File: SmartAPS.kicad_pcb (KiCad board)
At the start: 2 copper layers, 130 x 60 mm, 102 parts, among them M1 Mechanical-NC, M2 Mechanical-NC, M3 Mechanical-NC, M4 Mechanical, P1 12V IN, P2 GND, P3 OUT1, P4 OUT2, P5 USB_C_Receptacle_16P, P6 JESP32-DBG, Q1 MMBT5551, Q2 DMP3013SFV, Q3 MMBT5551, Q4 DMP3013SFV, Q5 MMBT5551, Q6 DMP3013SFV, Q7 TEMT6000X01, Q8 MMBT5551, U1 MCP1703T-3302E/MB, U2 MUN12AD01-SH, U3 INA226, U4 INA226, U5 IP6510, U6 INA226, U7 SHT20, U8 ESP32-WROOM-32U, U9 STM1001RWX6F

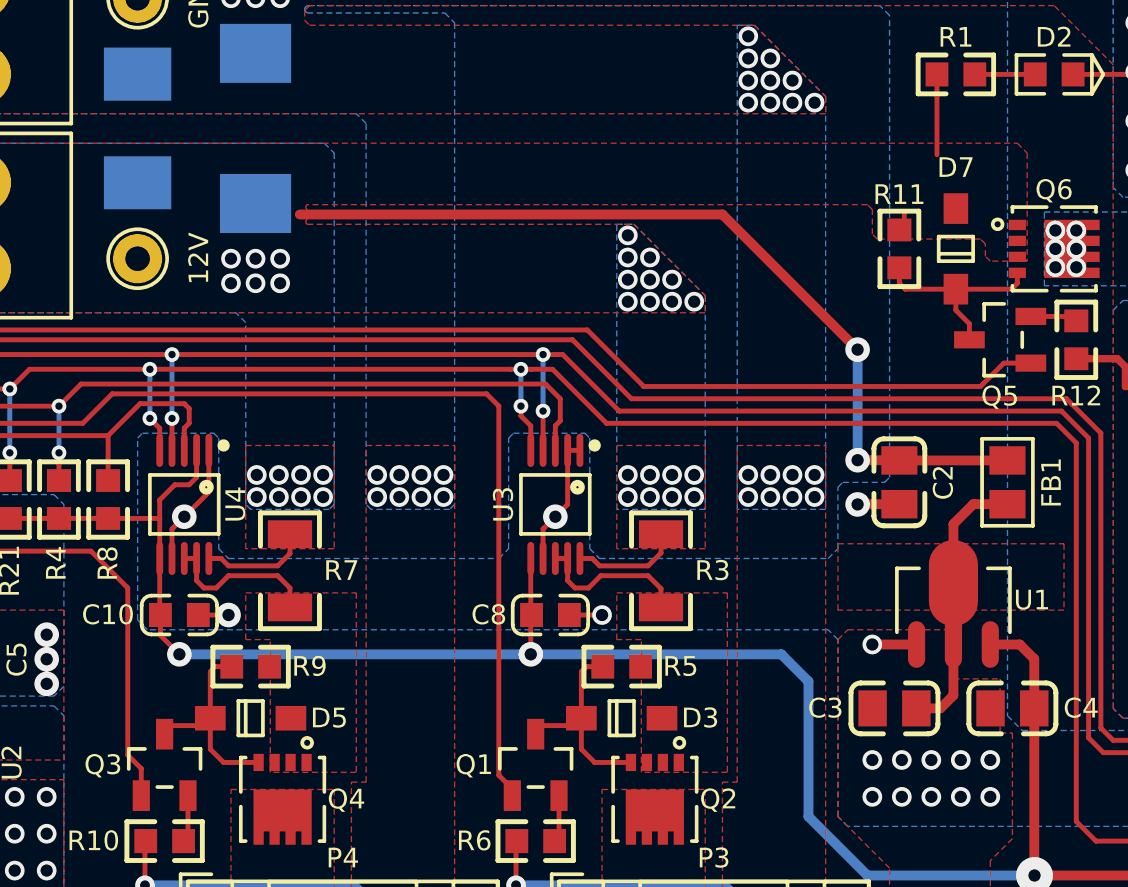
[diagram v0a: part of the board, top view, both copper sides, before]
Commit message: Solve INA226/SHT20 address clash
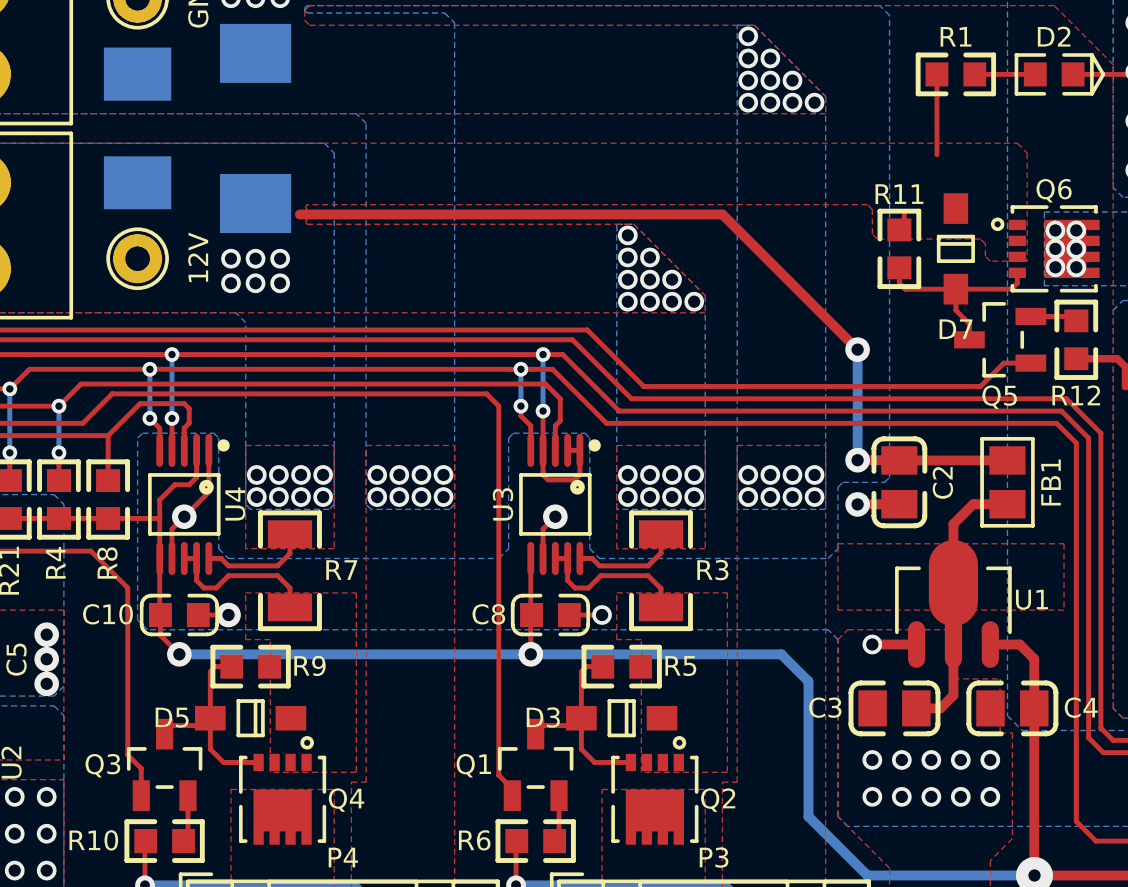
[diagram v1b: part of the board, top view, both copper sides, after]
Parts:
- turned D3 to 180 degrees
- turned D5 to 180 degrees
- turned D7 to 270 degrees
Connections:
- U3 pad 1: GND -> /SDA
- U3 pad 2: GND -> /SDA
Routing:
- net /SDA: track 156.1 -> 160.2 mm
- net GND: track 202.6 -> 199.2 mm

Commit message: Bug fixes, Remove SHT20
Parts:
- removed the C22 at (111.0, 86.0)
- removed the C25 at (226.1, 113.0)
- removed the TP4 at (210.7, 105.1)
- removed the TP5 at (208.7, 105.1)
- removed TP8: SCL, BZ_Misc:TE_RCT0805
- removed TP9: SDA, BZ_Misc:TE_RCT0805
- removed the U7 at (223.0, 113.0)
- added P7: Grove I2C, BZ_Connector:JST_S4B-PH-SM4-TB, F.Cu at (225.0, 116.5)
- added R23: 10K, BZ_Resistor:R_0603, F.Cu at (140.3, 124.2)
- added R24: 10K, BZ_Resistor:R_0603, F.Cu at (142.8, 124.2)
- moved C20 15.0 mm to (202.7, 120.0)
- moved C12 0.40 mm to (201.4, 83.0)
- moved C13 0.40 mm to (201.4, 88.6)
- moved C17 0.40 mm to (201.4, 97.0)
- turned S1 to 0 degrees
- renumbered C23 to C22, C24 to C23, C26 to C24, C27 to C25, C28 to C26, TP6 to TP4, TP7 to TP5, U8 to U7, U9 to U8
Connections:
- C20 pad 2: /SW1 -> /SW2
- C21 pad 2: /SW2 -> /SW3
- DISP1 pad 3: Net-(DISP1-Pad3) -> (no net)
- DISP1 pad 6: Net-(DISP1-Pad6) -> (no net)
- P5 pad A8: Net-(P5-PadA8) -> (no net)
- P5 pad B8: Net-(P5-PadB8) -> (no net)
- P6 pad 4: /TDI -> /TCK
- P6 pad 8: /TCK -> /TDI
- Q7 pad B: Net-(Q7-PadB) -> (no net)
- S2 pad 1: /SW1 -> /SW2
- S3 pad 1: /SW2 -> /SW3
- U2 pad 1: Net-(U2-Pad1) -> (no net)
- U2 pad 3: Net-(U2-Pad3) -> (no net)
- U2 pad 6: Net-(U2-Pad6) -> (no net)
- U7 pad 10: /PWR1 -> /BUZ
- U7 pad 11: /ALT1 -> /PWR1
- U7 pad 12: /BUZ -> /ALT1
- U7 pad 17: Net-(U8-Pad17) -> (no net)
- U7 pad 18: Net-(U8-Pad18) -> (no net)
- U7 pad 19: Net-(U8-Pad19) -> (no net)
- U7 pad 20: Net-(U8-Pad20) -> (no net)
- U7 pad 21: Net-(U8-Pad21) -> (no net)
- U7 pad 22: Net-(U8-Pad22) -> (no net)
- U7 pad 24: /IR -> (no net)
- U7 pad 32: Net-(U8-Pad32) -> (no net)
- U7 pad 5: Net-(U8-Pad5) -> (no net)
- U7 pad 6: /SW1 -> /SW2
- U7 pad 7: /SW2 -> /SW3
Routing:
- net /SW1: track 122.0 -> 0.00 mm, vias 1 -> 0
- net GND: track 199.2 -> 296.2 mm, vias 196 -> 192
- net /SW3: track 0.00 -> 88.2 mm, vias 0 -> 1
- net /SW2: track 82.9 -> 127.1 mm
- net 3V3: track 117.8 -> 137.0 mm
- net /SDA: track 160.2 -> 174.6 mm
- net VDDA: track 141.0 -> 128.0 mm, vias 6 -> 3
- net /IO0: track 51.6 -> 43.0 mm
- net /SCL: track 162.5 -> 170.6 mm
- net /TDI: track 20.3 -> 15.3 mm
- net /TCK: track 19.4 -> 23.5 mm, vias 0 -> 2
- net /TDO: track 33.9 -> 30.1 mm
- net Net-(D3-PadK): track 6.51 -> 9.36 mm
- net Net-(D5-PadK): track 6.53 -> 9.38 mm
- net /PWR1: track 100.7 -> 98.6 mm
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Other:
- outline, holes or cut-outs redrawn
- board text added: "20200510"
- board text added: "GND"
- board text added: "OUT_A"
- board text added: "OUT_B"
- board text added: "SCL"
- board text added: "SDA"
- board text added: "VCC"
- board text removed: "20200402"
- board text removed: "OUT1"
- board text removed: "OUT2"
